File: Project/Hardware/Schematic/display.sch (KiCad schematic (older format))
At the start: 4 parts

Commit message: Fixa bibliotek ref
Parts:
- U?: symbol lab-rescue:DEM16220SYM-PASC -> PASC:DEM16220SYM
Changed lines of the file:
@@
 	1250 2750 1200 2750
 $Comp
-L lab-rescue:DEM16220SYM-PASC U?
+L PASC:DEM16220SYM U?
 U 1 1 5C69A8D5
 P 4500 1900

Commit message: Bytte display
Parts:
- removed U?: DEM16220SYM, symbol PASC:DEM16220SYM
- added C?: C, symbol Device:C
- added R?: R, symbol Device:R
- added U?: OLED-128O064D, symbol PASC:OLED-128O064D
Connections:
- net labels added: LCD_BS0, LCD_BS1, LCD_BS2, LCD_DC, LCD_RES, LCD_SCL, LCD_SDA
- net labels removed: LCD_DB0, LCD_DB1, LCD_DB2, LCD_DB3, LCD_DB4, LCD_DB5, LCD_DB6, LCD_DB7, LCD_RS, LCS_VDD, V0
- wire segments 13 -> 20
- no-connect marks 0 -> 9
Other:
- note removed: "Connector to flatcable for display."
- moved on the sheet: C?, Q?, R?

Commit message: Ny display, igen!
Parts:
- removed C?: C, symbol Device:C
- removed U?: OLED-128O064D, symbol PASC:OLED-128O064D
- added R? (x4): 1k, symbol Device:R
- added U?: Oled-MCTO, symbol PASC:Oled-MCTO
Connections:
- net labels added: +3.3V, +3V3, BS1, BS2, C1N, C1P, C2N, C2P, CS, DC
- net labels removed: LCD_BS0, LCD_BS1, LCD_BS2
- wire segments 20 -> 26
- no-connect marks 9 -> 5
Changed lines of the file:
@@
 $EndDescr
-$Comp
-L power:+5V #PWR?
-U 1 1 5C58DDEB
-P 850 1000
-F 0 "#PWR?" H 850 850 50  0001 C CNN
-F 1 "+5V" H 865 1173 50  0000 C CNN
-F 2 "" H 850 1000 50  0001 C CNN
-F 3 "" H 850 1000 50  0001 C CNN
-	1    850  1000
-	1    0    0    -1
-$EndComp
 $Comp
 L power:GND #PWR?
@@
 LCD_BACKLIGHT
 $Comp
-L PASC:OLED-128O064D U?
-U 1 1 5C5E0371
-P 4800 1600
-F 0 "U?" H 4700 -800 50  0000 L CNN
-F 1 "OLED-128O064D" H 4600 -650 50  0000 L CNN
-F 2 "" H 4850 1600 50  0001 C CNN
-F 3 "" H 4850 1600 50  0001 C CNN
-	1    4800 1600
-	1    0    0    -1
-$EndComp
-$Comp
 L power:GND #PWR?
 U 1 1 5C5E07BD
-P 1750 1650
-F 0 "#PWR?" H 1750 1400 50  0001 C CNN
-F 1 "GND" H 1755 1477 50  0000 C CNN
-F 2 "" H 1750 1650 50  0001 C CNN
-F 3 "" H 1750 1650 50  0001 C CNN
-	1    1750 1650
-	1    0    0    -1
-$EndComp
-Wire Wire Line
-	1750 1650 1750 1550
-Text Label 1750 1550 0    50   ~ 0
+P 1350 1850
+F 0 "#PWR?" H 1350 1600 50  0001 C CNN
+F 1 "GND" H 1355 1677 50  0000 C CNN
+F 2 "" H 1350 1850 50  0001 C CNN
+F 3 "" H 1350 1850 50  0001 C CNN
+	1    1350 1850
+	1    0    0    -1
+$EndComp
+Wire Wire Line
+	1350 1850 1350 1750
+Text Label 1350 1750 0    50   ~ 0
 GND
 Text Label 4250 750  2    50   ~ 0
 GND
-Text Label 4250 3650 2    50   ~ 0
+Text Label 4250 3450 2    50   ~ 0
 GND
-Text Label 4250 1250 2    50   ~ 0
-LCD_VDD
-Text Label 4250 1450 2    50   ~ 0
+Text Label 4250 1350 2    50   ~ 0
 LCD_VSS
-Text Label 4250 1550 2    50   ~ 0
-LCD_VDD
-Text HLabel 4250 1650 0    50   Input ~ 0
-LCD_BS0
-Text HLabel 4250 1750 0    50   Input ~ 0
-LCD_BS1
-Text HLabel 4250 1850 0    50   Input ~ 0
-LCD_BS2
-Text Label 4250 1950 2    50   ~ 0
-GND
 Text HLabel 4250 2050 0    50   Input ~ 0
 LCD_RES
@@
 Text Label 3350 2950 0    50   ~ 0
 LCD_VSS
-$Comp
-L Device:C C?
-U 1 1 5C5E0CC4
-P 3000 3100
-F 0 "C?" H 3115 3146 50  0000 L CNN
-F 1 "C" H 3115 3055 50  0000 L CNN
-F 2 "" H 3038 2950 50  0001 C CNN
-F 3 "~" H 3000 3100 50  0001 C CNN
-	1    3000 3100
-	1    0    0    -1
-$EndComp
-Wire Wire Line
-	4250 3350 3000 3350
-Text Label 3000 2950 0    50   ~ 0
-LCD_VSS
-Wire Wire Line
-	3000 3250 3000 3350
-Text Label 4250 3450 2    50   ~ 0
-LCD_VDD
-Text Label 4250 3550 2    50   ~ 0
-LCD_VSS
-NoConn ~ 4250 850
-NoConn ~ 4250 950
-NoConn ~ 4250 1050
-NoConn ~ 4250 1150
 Wire Wire Line
 	4250 2550 4100 2550
@@
 NoConn ~ 4250 3050
 NoConn ~ 4250 3150
+$Comp
+L power:+3.3V #PWR?
+U 1 1 5C66DBDE
+P 850 1000
+F 0 "#PWR?" H 850 850 50  0001 C CNN
+F 1 "+3.3V" H 865 1173 50  0000 C CNN
+F 2 "" H 850 1000 50  0001 C CNN
+F 3 "" H 850 1000 50  0001 C CNN
+	1    850  1000
+	1    0    0    -1
+$EndComp
+$Comp
+L PASC:Oled-MCTO U?
+U 1 1 5C67BD88
+P 4800 2200
+F 0 "U?" H 5277 2221 50  0000 L CNN
+F 1 "Oled-MCTO" H 5277 2130 50  0000 L CNN
+F 2 "" H 4800 2200 50  0001 C CNN
+F 3 "" H 4800 2200 50  0001 C CNN
+	1    4800 2200
+	1    0    0    -1
+$EndComp
+Text Label 4250 850  2    50   ~ 0
+C2P
+Text Label 4250 950  2    50   ~ 0
+C2N
+Text Label 4250 1050 2    50   ~ 0
+C1P
+Text Label 4250 1150 2    50   ~ 0
+C1N
+Text Label 4250 1250 2    50   ~ 0
+LCD_VDD
+Text Label 4250 1450 2    50   ~ 0
+LCD_VDD
+Text HLabel 4250 1850 0    50   Input ~ 0
+LCD_RES
+$Comp
+L power:+3V3 #PWR?
+U 1 1 5C67D4BA
+P 3000 1100
+F 0 "#PWR?" H 3000 950 50  0001 C CNN
+F 1 "+3V3" H 3015 1273 50  0000 C CNN
+F 2 "" H 3000 1100 50  0001 C CNN
+F 3 "" H 3000 1100 50  0001 C CNN
+	1    3000 1100
+	1    0    0    -1
+$EndComp
+$Comp
+L Device:R R?
+U 1 1 5C67D500
+P 3000 1400
+F 0 "R?" H 3070 1446 50  0000 L CNN
+F 1 "1k" H 3070 1355 50  0000 L CNN
+F 2 "" V 2930 1400 50  0001 C CNN
+F 3 "~" H 3000 1400 50  0001 C CNN
+	1    3000 1400
+	1    0    0    -1
+$EndComp
+Wire Wire Line
+	3000 1100 3000 1250
+Wire Wire Line
+	3000 1550 3000 1700
+Text Label 3000 1700 0    50   ~ 0
+BS1
+$Comp
+L Device:R R?
+U 1 1 5C67D7C1
+P 2700 1400
+F 0 "R?" H 2770 1446 50  0000 L CNN
+F 1 "1k" H 2770 1355 50  0000 L CNN
+F 2 "" V 2630 1400 50  0001 C CNN
+F 3 "~" H 2700 1400 50  0001 C CNN
+	1    2700 1400
+	1    0    0    -1
+$EndComp
+Wire Wire Line
+	2700 1250 2700 1100
+Text Label 2700 1100 0    50   ~ 0
+BS2
+$Comp
+L power:GND #PWR?
+U 1 1 5C67D9C3
+P 2450 1700
+F 0 "#PWR?" H 2450 1450 50  0001 C CNN
+F 1 "GND" H 2455 1527 50  0000 C CNN
+F 2 "" H 2450 1700 50  0001 C CNN
+F 3 "" H 2450 1700 50  0001 C CNN
+	1    2450 1700
+	1    0    0    -1
+$EndComp
+Wire Wire Line
+	2450 1550 2450 1700
+Text Label 4250 1550 2    50   ~ 0
+BS1
+Text Label 4250 1650 2    50   ~ 0
+BS2
+$Comp
+L Device:R R?
+U 1 1 5C67E312
+P 2450 1400
+F 0 "R?" H 2520 1446 50  0000 L CNN
+F 1 "1k" H 2520 1355 50  0000 L CNN
+F 2 "" V 2380 1400 50  0001 C CNN
+F 3 "~" H 2450 1400 50  0001 C CNN
+	1    2450 1400
+	1    0    0    -1
+$EndComp
+$Comp
+L power:GND #PWR?
+U 1 1 5C67E539
+P 2700 1700
+F 0 "#PWR?" H 2700 1450 50  0001 C CNN
+F 1 "GND" H 2705 1527 50  0000 C CNN
+F 2 "" H 2700 1700 50  0001 C CNN
+F 3 "" H 2700 1700 50  0001 C CNN
+	1    2700 1700
+	1    0    0    -1
+$EndComp
+Wire Wire Line
+	2700 1700 2700 1550
+Wire Wire Line
+	2450 1250 2450 1100
+Text Label 2450 1100 0    50   ~ 0
+DC
+Text Label 4250 1950 2    50   ~ 0
+DC
+$Comp
+L power:GND #PWR?
+U 1 1 5C67ED6A
+P 2200 1700
+F 0 "#PWR?" H 2200 1450 50  0001 C CNN
+F 1 "GND" H 2205 1527 50  0000 C CNN
+F 2 "" H 2200 1700 50  0001 C CNN
+F 3 "" H 2200 1700 50  0001 C CNN
+	1    2200 1700
+	1    0    0    -1
+$EndComp
+Wire Wire Line
+	2200 1550 2200 1700
+$Comp
+L Device:R R?
+U 1 1 5C67ED71
+P 2200 1400
+F 0 "R?" H 2270 1446 50  0000 L CNN
+F 1 "1k" H 2270 1355 50  0000 L CNN
+F 2 "" V 2130 1400 50  0001 C CNN
+F 3 "~" H 2200 1400 50  0001 C CNN
+	1    2200 1400
+	1    0    0    -1
+$EndComp
+Wire Wire Line
+	2200 1250 2200 1100
+Text Label 2200 1100 0    50   ~ 0
+CS
+Text Label 4250 1750 2    50   ~ 0
+CS
 $EndSCHEMATC

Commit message: Buttons och display
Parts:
- removed Q?: BSS138, Package_TO_SOT_SMD:SOT-23, symbol Transistor_FET:BSS138
- removed R?: 100, symbol Device:R
- removed R?: R, symbol Device:R
- added C?: 2.2u, symbol Device:C
- added C?: C, symbol Device:C
- added R?: 330, symbol Device:R
- added R?: 33, symbol Device:R
- added RV?: R_POT, symbol Device:R_POT
- C?: value 2.2u -> 1u
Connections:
- net LCD_DC is gone; now on net LCD_E: U?.15 (E)
- net GND: now also C?.1, C?.2, C?.2, RV?.3
- net LCD_E: no longer U?.17 (DB1)
- net LCD_RES: no longer U?.14 (RW)
- net LCD_RW: now also U?.14 (RW); no longer U?.16 (DB0)
- net LCD_SCL: now also U?.16 (DB0); no longer U?.18 (DB2)
- net LCD_SDA: now also U?.17 (DB1), U?.18 (DB2); no longer U?.19 (DB3), U?.20 (DB4)
- net LCD_VCC: now reaches U?.26 (VCC)
- net IREF: now reaches U?.24 (IREF)
- net IREF: now also R?.1
- net VCOMH: now reaches U?.25 (VCOMH)
- net VCOMH: now also C?.1
- net LCS_VSS: now reaches U?.27 (VLSS)
- new net: R?.1, R?.2
- new net: R?.2, RV?.1
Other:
- moved on the sheet: U?
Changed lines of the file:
@@
 P 850 1300
 F 0 "C?" H 965 1346 50  0000 L CNN
-F 1 "2.2u" H 965 1255 50  0000 L CNN
+F 1 "1u" H 965 1255 50  0000 L CNN
 F 2 "" H 888 1150 50  0001 C CNN
 F 3 "~" H 850 1300 50  0001 C CNN
@@
 LCD_VSS
 $Comp
-L Transistor_FET:BSS138 Q?
-U 1 1 5C58DFD0
-P 1900 2600
-F 0 "Q?" H 2105 2646 50  0000 L CNN
-F 1 "BSS138" H 2105 2555 50  0000 L CNN
-F 2 "Package_TO_SOT_SMD:SOT-23" H 2100 2525 50  0001 L CIN
-F 3 "https://www.fairchildsemi.com/datasheets/BS/BSS138.pdf" H 1900 2600 50  0001 L CNN
-	1    1900 2600
-	1    0    0    -1
-$EndComp
-Wire Wire Line
-	2000 2400 2000 2300
-Wire Wire Line
-	2000 2800 2000 2900
-$Comp
-L Device:R R?
-U 1 1 5C58E912
-P 1500 2600
-F 0 "R?" V 1400 2600 50  0000 C CNN
-F 1 "100" V 1600 2600 50  0000 C CNN
-F 2 "" V 1430 2600 50  0001 C CNN
-F 3 "~" H 1500 2600 50  0001 C CNN
-	1    1500 2600
-	0    1    1    0
-$EndComp
-Wire Wire Line
-	1700 2600 1650 2600
-Wire Wire Line
-	1350 2600 1300 2600
-$Comp
-L power:+5V #PWR?
-U 1 1 5C5BE7E6
-P 2000 2300
-F 0 "#PWR?" H 2000 2150 50  0001 C CNN
-F 1 "+5V" H 2015 2473 50  0000 C CNN
-F 2 "" H 2000 2300 50  0001 C CNN
-F 3 "" H 2000 2300 50  0001 C CNN
-	1    2000 2300
-	1    0    0    -1
-$EndComp
-Wire Wire Line
-	2000 2900 2100 2900
-Text Label 2100 2900 0    50   ~ 0
-LCD_VLED+
-Text Label 2100 3100 0    50   ~ 0
-LCD_VLED-
-Wire Wire Line
-	2000 3100 2100 3100
-$Comp
-L power:GND #PWR?
-U 1 1 5C5BF407
-P 2000 3400
-F 0 "#PWR?" H 2000 3150 50  0001 C CNN
-F 1 "GND" H 2005 3227 50  0000 C CNN
-F 2 "" H 2000 3400 50  0001 C CNN
-F 3 "" H 2000 3400 50  0001 C CNN
-	1    2000 3400
-	1    0    0    -1
-$EndComp
-Wire Wire Line
-	2000 3100 2000 3400
-Text HLabel 1300 2600 0    50   Input ~ 0
-LCD_BACKLIGHT
-$Comp
 L power:GND #PWR?
 U 1 1 5C5E07BD
-P 1350 1850
-F 0 "#PWR?" H 1350 1600 50  0001 C CNN
-F 1 "GND" H 1355 1677 50  0000 C CNN
-F 2 "" H 1350 1850 50  0001 C CNN
-F 3 "" H 1350 1850 50  0001 C CNN
-	1    1350 1850
-	1    0    0    -1
-$EndComp
-Wire Wire Line
-	1350 1850 1350 1750
-Text Label 1350 1750 0    50   ~ 0
+P 850 2100
+F 0 "#PWR?" H 850 1850 50  0001 C CNN
+F 1 "GND" H 855 1927 50  0000 C CNN
+F 2 "" H 850 2100 50  0001 C CNN
+F 3 "" H 850 2100 50  0001 C CNN
+	1    850  2100
+	1    0    0    -1
+$EndComp
+Wire Wire Line
+	850  2100 850  2000
+Text Label 850  2000 0    50   ~ 0
 GND
-Text Label 4250 750  2    50   ~ 0
+Text Label 4100 750  2    50   ~ 0
 GND
-Text Label 4250 3450 2    50   ~ 0
-GND
-Text Label 4250 1350 2    50   ~ 0
-LCD_VSS
-Text HLabel 4250 2050 0    50   Input ~ 0
-LCD_RES
-Text HLabel 4250 2150 0    50   Input ~ 0
-LCD_DC
-Text HLabel 4250 2250 0    50   Input ~ 0
+Text Label 4100 1350 2    50   ~ 0
+LCD_VSS
+Text HLabel 4100 2050 0    50   Input ~ 0
 LCD_RW
-Text HLabel 4250 2350 0    50   Input ~ 0
+Text HLabel 4100 2150 0    50   Input ~ 0
 LCD_E
-$Comp
-L Device:R R?
-U 1 1 5C5E0B06
-P 3350 3100
-F 0 "R?" H 3420 3146 50  0000 L CNN
-F 1 "R" H 3420 3055 50  0000 L CNN
-F 2 "" V 3280 3100 50  0001 C CNN
-F 3 "~" H 3350 3100 50  0001 C CNN
-	1    3350 3100
-	1    0    0    -1
-$EndComp
-Wire Wire Line
-	4250 3250 3350 3250
-Text Label 3350 2950 0    50   ~ 0
-LCD_VSS
-Wire Wire Line
-	4250 2550 4100 2550
-Wire Wire Line
-	4100 2550 4100 2650
-Wire Wire Line
-	4100 2650 4250 2650
-Text HLabel 4100 2600 0    50   Input ~ 0
+Wire Wire Line
+	4100 2350 3950 2350
+Wire Wire Line
+	3950 2350 3950 2450
+Wire Wire Line
+	3950 2450 4100 2450
+Text HLabel 3950 2400 0    50   Input ~ 0
 LCD_SDA
-Text HLabel 4250 2450 0    50   Input ~ 0
+Text HLabel 4100 2250 0    50   Input ~ 0
 LCD_SCL
-NoConn ~ 4250 2750
-NoConn ~ 4250 2850
-NoConn ~ 4250 2950
-NoConn ~ 4250 3050
-NoConn ~ 4250 3150
+NoConn ~ 4100 2750
+NoConn ~ 4100 2850
+NoConn ~ 4100 2950
 $Comp
 L power:+3.3V #PWR?
@@
 L PASC:Oled-MCTO U?
 U 1 1 5C67BD88
-P 4800 2200
-F 0 "U?" H 5277 2221 50  0000 L CNN
-F 1 "Oled-MCTO" H 5277 2130 50  0000 L CNN
-F 2 "" H 4800 2200 50  0001 C CNN
-F 3 "" H 4800 2200 50  0001 C CNN
-	1    4800 2200
-	1    0    0    -1
-$EndComp
-Text Label 4250 850  2    50   ~ 0
+P 4650 2200
+F 0 "U?" H 4750 450 50  0000 L CNN
+F 1 "Oled-MCTO" H 4550 550 50  0000 L CNN
+F 2 "" H 4650 2200 50  0001 C CNN
+F 3 "" H 4650 2200 50  0001 C CNN
+	1    4650 2200
+	1    0    0    -1
+$EndComp
+Text Label 4100 850  2    50   ~ 0
 C2P
-Text Label 4250 950  2    50   ~ 0
+Text Label 4100 950  2    50   ~ 0
 C2N
-Text Label 4250 1050 2    50   ~ 0
+Text Label 4100 1050 2    50   ~ 0
 C1P
-Text Label 4250 1150 2    50   ~ 0
+Text Label 4100 1150 2    50   ~ 0
 C1N
-Text Label 4250 1250 2    50   ~ 0
+Text Label 4100 1250 2    50   ~ 0
 LCD_VDD
-Text Label 4250 1450 2    50   ~ 0
+Text Label 4100 1450 2    50   ~ 0
 LCD_VDD
-Text HLabel 4250 1850 0    50   Input ~ 0
+Text HLabel 4100 1850 0    50   Input ~ 0
 LCD_RES
-$Comp
-L power:+3V3 #PWR?
-U 1 1 5C67D4BA
-P 3000 1100
-F 0 "#PWR?" H 3000 950 50  0001 C CNN
-F 1 "+3V3" H 3015 1273 50  0000 C CNN
-F 2 "" H 3000 1100 50  0001 C CNN
-F 3 "" H 3000 1100 50  0001 C CNN
-	1    3000 1100
-	1    0    0    -1
-$EndComp
 $Comp
 L Device:R R?
@@
 Wire Wire Line
 	2450 1550 2450 1700
-Text Label 4250 1550 2    50   ~ 0
+Text Label 4100 1550 2    50   ~ 0
 BS1
-Text Label 4250 1650 2    50   ~ 0
+Text Label 4100 1650 2    50   ~ 0
 BS2
 $Comp
@@
 Text Label 2450 1100 0    50   ~ 0
 DC
-Text Label 4250 1950 2    50   ~ 0
+Text Label 4100 1950 2    50   ~ 0
 DC
 $Comp
@@
 Text Label 2200 1100 0    50   ~ 0
 CS
-Text Label 4250 1750 2    50   ~ 0
+Text Label 4100 1750 2    50   ~ 0
 CS
+NoConn ~ 4100 2550
+NoConn ~ 4100 2650
+$Comp
+L Device:R R?
+U 1 1 5C684477
+P 2300 2950
+F 0 "R?" H 2370 2996 50  0000 L CNN
+F 1 "330" H 2370 2905 50  0000 L CNN
+F 2 "" V 2230 2950 50  0001 C CNN
+F 3 "~" H 2300 2950 50  0001 C CNN
+	1    2300 2950
+	1    0    0    -1
+$EndComp
+$Comp
+L Device:R R?
+U 1 1 5C6844F9
+P 2300 3350
+F 0 "R?" H 2370 3396 50  0000 L CNN
+F 1 "33" H 2370 3305 50  0000 L CNN
+F 2 "" V 2230 3350 50  0001 C CNN
+F 3 "~" H 2300 3350 50  0001 C CNN
+	1    2300 3350
+	1    0    0    -1
+$EndComp
+Wire Wire Line
+	2300 3100 2300 3200
+$Comp
+L Device:R_POT RV?
+U 1 1 5C684AC3
+P 2300 3750
+F 0 "RV?" H 2230 3796 50  0000 R CNN
+F 1 "R_POT" H 2230 3705 50  0000 R CNN
+F 2 "" H 2300 3750 50  0001 C CNN
+F 3 "~" H 2300 3750 50  0001 C CNN
+	1    2300 3750
+	1    0    0    -1
+$EndComp
+Wire Wire Line
+	2300 3600 2300 3500
+Text Label 4100 3250 2    50   ~ 0
+LCD_VCC
+Wire Wire Line
+	2300 3900 2300 4050
+Text Label 2300 4050 0    50   ~ 0
+LCD_VSS
+Text Label 4100 3050 2    50   ~ 0
+IREF
+Wire Wire Line
+	2300 2800 2300 2650
+Text Label 2300 2650 0    50   ~ 0
+IREF
+$Comp
+L Device:C C?
+U 1 1 5C685FEC
+P 2850 2900
+F 0 "C?" H 2965 2946 50  0000 L CNN
+F 1 "2.2u" H 2965 2855 50  0000 L CNN
+F 2 "" H 2888 2750 50  0001 C CNN
+F 3 "~" H 2850 2900 50  0001 C CNN
+	1    2850 2900
+	1    0    0    -1
+$EndComp
+Wire Wire Line
+	2850 2750 2850 2650
+Text Label 2850 2650 0    50   ~ 0
+VCOMH
+Wire Wire Line
+	2850 3050 2850 3250
+Text Label 2850 3250 0    50   ~ 0
+LCD_VSS
+Text Label 4100 3450 2    50   ~ 0
+GND
+Text Label 4100 3150 2    50   ~ 0
+VCOMH
+Text Label 4100 3350 2    50   ~ 0
+LCS_VSS
+Text Label 3000 1100 0    50   ~ 0
+LCD_VDD
+$Comp
+L Device:C C?
+U 1 1 5C689C8F
+P 850 3150
+F 0 "C?" H 965 3196 50  0000 L CNN
+F 1 "C" H 965 3105 50  0000 L CNN
+F 2 "" H 888 3000 50  0001 C CNN
+F 3 "~" H 850 3150 50  0001 C CNN
+	1    850  3150
+	1    0    0    -1
+$EndComp
+Wire Wire Line
+	850  2900 850  3000
+Wire Wire Line
+	850  2900 1050 2900
+Text Label 1050 2900 0    50   ~ 0
+LCD_VSS
+Wire Wire Line
+	850  3300 850  3450
+Text Label 850  3450 0    50   ~ 0
+LCD_VSS
 $EndSCHEMATC

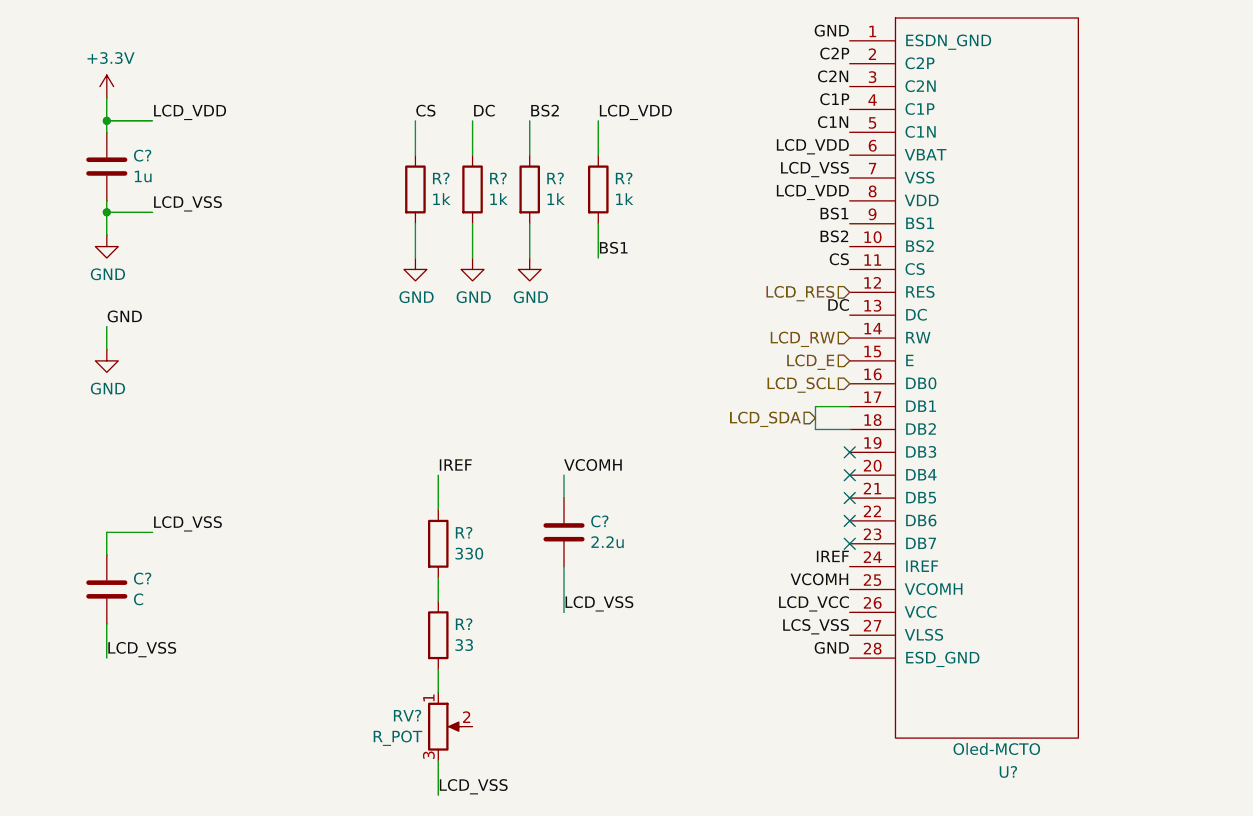
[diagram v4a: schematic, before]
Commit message: Display footprint
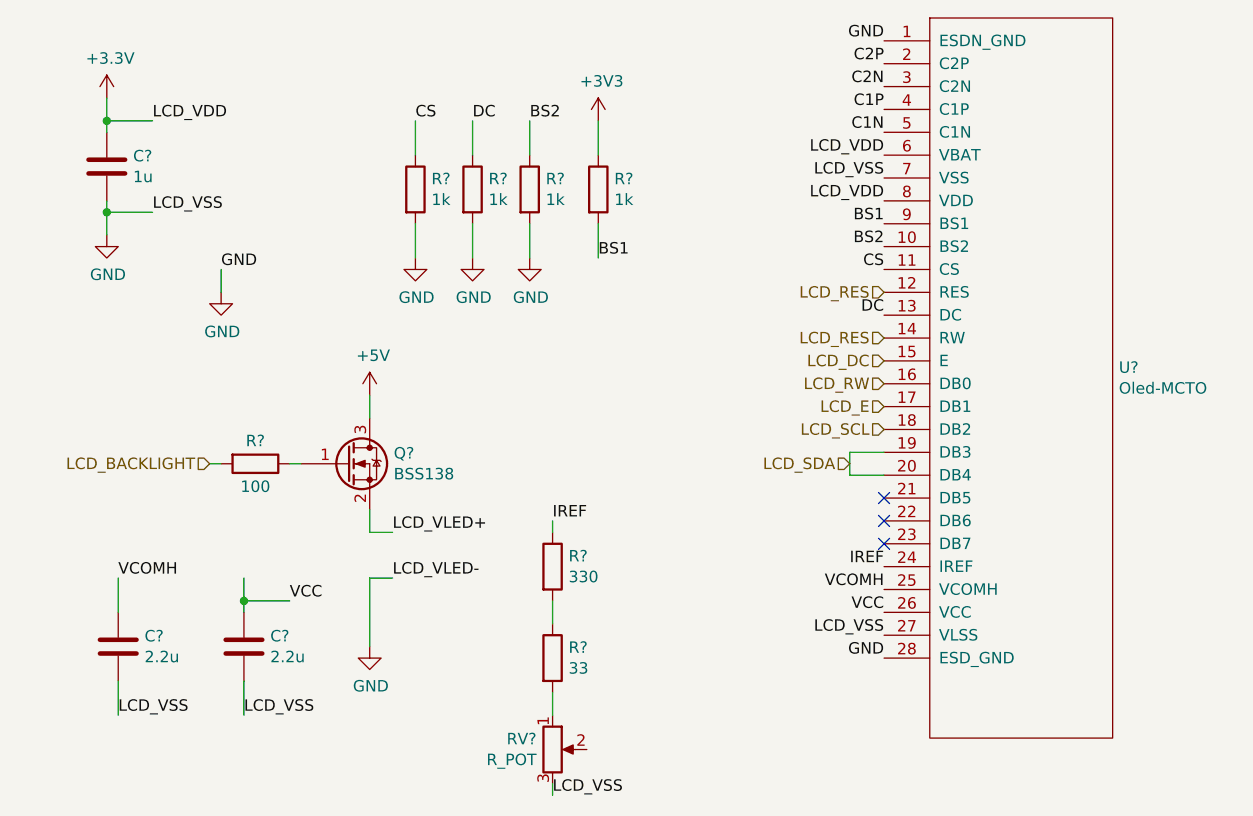
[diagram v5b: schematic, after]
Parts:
- removed C?: 2.2u, symbol Device:C
- removed C?: C, symbol Device:C
- removed R?: 330, symbol Device:R
- removed R?: 33, symbol Device:R
- removed RV?: R_POT, symbol Device:R_POT
- added C? (x2): 2.2u, symbol Device:C
- added Q?: BSS138, Package_TO_SOT_SMD:SOT-23, symbol Transistor_FET:BSS138
- added R?: 100, symbol Device:R
- added R?: 330, symbol Device:R
- added R?: 33, symbol Device:R
- added RV?: R_POT, symbol Device:R_POT
- U?: footprint (none) -> PASC:MCOT064048A1V
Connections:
- net LCS_VSS is gone; now on net GND: U?.27 (VLSS)
- net GND: now also C?.2, C?.2, RV?.3
- net IREF: now also R?.1
- net LCD_E: now also U?.17 (DB1); no longer U?.15 (E)
- net LCD_RES: now also U?.14 (RW)
- net LCD_RW: now also U?.16 (DB0); no longer U?.14 (RW)
- net LCD_SCL: now also U?.18 (DB2); no longer U?.16 (DB0)
- net LCD_SDA: now also U?.19 (DB3), U?.20 (DB4); no longer U?.17 (DB1), U?.18 (DB2)
- net VCOMH: now also C?.1
- net LCD_VCC renamed VCC
- net VCC: now also C?.1
- new net: Q?.1 (G), R?.1
- new net: R?.1, R?.2
- new net: R?.2, RV?.1
- new net +5V: Q?.3 (D)
- new net LCD_BACKLIGHT: R?.2
- new net LCD_DC: U?.15 (E)
- new net LCD_VLED+: Q?.2 (S)
- no-connect marks 5 -> 3
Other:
- moved on the sheet: U?

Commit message: Display fix
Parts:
- removed C? (x2): 2.2u, symbol Device:C
- removed Q?: BSS138, Package_TO_SOT_SMD:SOT-23, symbol Transistor_FET:BSS138
- removed R?: 100, symbol Device:R
- removed R?: 330, symbol Device:R
- removed R?: 33, symbol Device:R
- removed RV?: R_POT, symbol Device:R_POT
- added C? (x2): 2.2u, symbol Device:C
- added R?: 330, symbol Device:R
- added R?: 33, symbol Device:R
- added RV?: R_POT, symbol Device:R_POT
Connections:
- net LCD_DC is gone; now on net LCD_E: U?.15 (E)
- net GND: now also C?.1, C?.2, C?.2, RV?.3; no longer U?.27 (VLSS)
- net IREF: now also R?.1
- net LCD_E: no longer U?.17 (DB1)
- net LCD_RES: no longer U?.14 (RW)
- net LCD_RW: now also U?.14 (RW); no longer U?.16 (DB0)
- net LCD_SCL: now also U?.16 (DB0); no longer U?.18 (DB2)
- net LCD_SDA: now also U?.17 (DB1), U?.18 (DB2); no longer U?.19 (DB3), U?.20 (DB4)
- net VCOMH: now also C?.1
- net VCC renamed LCD_VCC
- new net: R?.1, R?.2
- new net: R?.2, RV?.1
- new net LCS_VSS: U?.27 (VLSS)
- no-connect marks 3 -> 5
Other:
- moved on the sheet: U?
